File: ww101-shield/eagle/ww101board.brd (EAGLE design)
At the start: 53.3 x 60.6 mm, 6 parts, among them U1 LIGHTSENSORALS

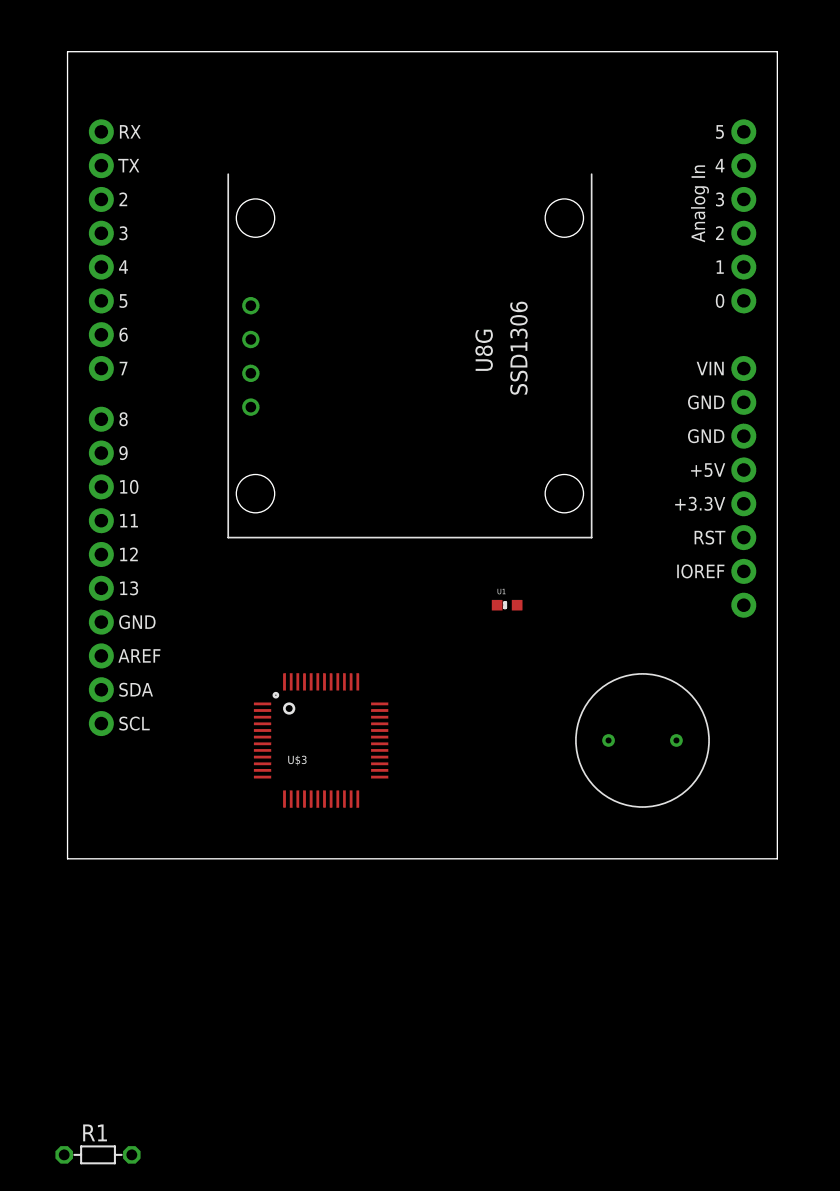
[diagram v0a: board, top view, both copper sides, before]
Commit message: Power routing done... now try signal routing
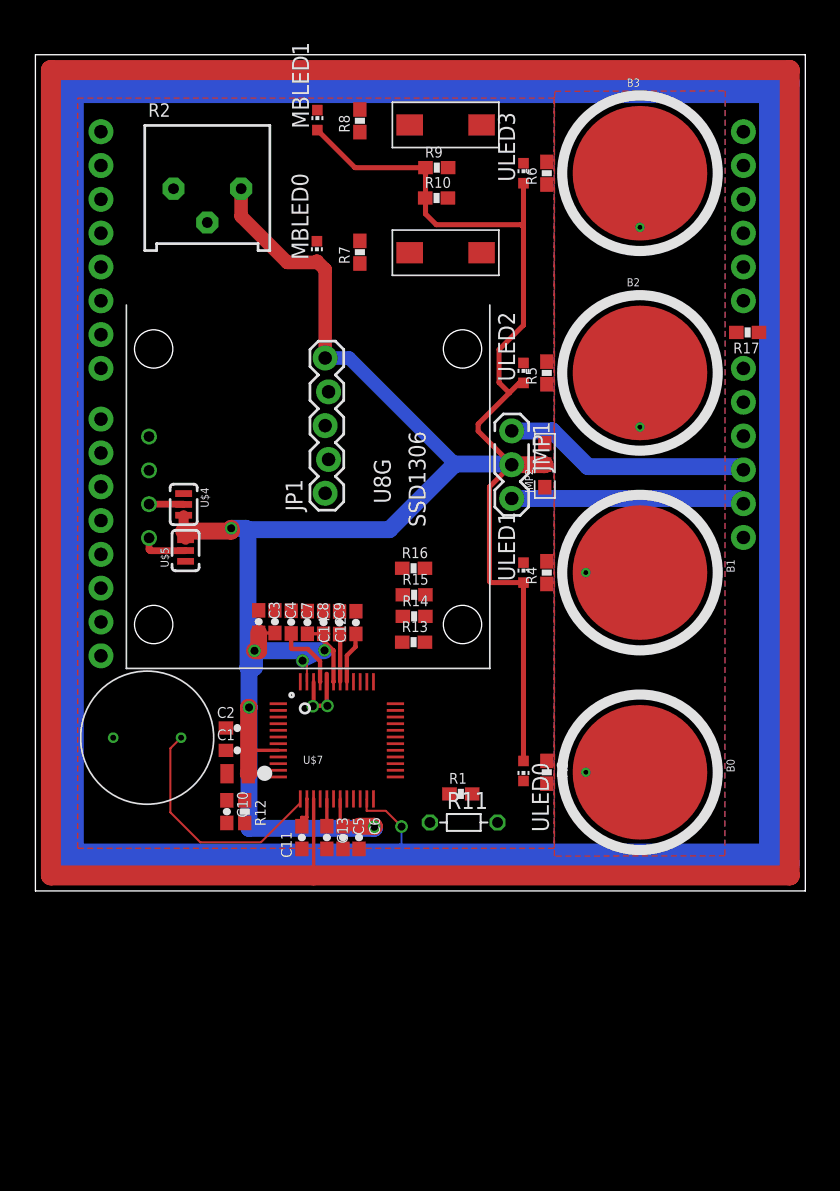
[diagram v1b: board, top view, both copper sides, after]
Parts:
- removed U$1: ARDUINO_R3_SHIELD, SparkFun-Boards:UNO_R3_SHIELD
- added ALS: ALS, IOTExpert:ALS
- added B0, B1, B2, B3: (no value), PatternAgents-TouchWidgets:BUTTON_PASSIVE_10MM
- added C1, C3, C5, C8: 1uF, PatternAgents-ProtoPads:0603-CAP
- added C10, C2, C4, C6, C7, C9: 0.1uF, PatternAgents-ProtoPads:0603-CAP
- added C11: 180pF, PatternAgents-ProtoPads:0603-CAP
- added C12, C13, C14: (no value), PatternAgents-ProtoPads:0603-CAP
- added JMP1: (no value), PatternAgents-ProtoPads:JMP-3-NO-PTH-2.54
- added JMP2: (no value), PatternAgents-ProtoPads:JMP-3-NO-0603
- added JP1: (no value), SparkFun-Connectors:1X05_LOCK
- added MB0, MB1: EVQPE1, IOTExpert:SWITCH
- added MBLED0, MBLED1, ULED0, ULED1, ULED2, ULED3: (no value), adafruit:CHIP-LED0603
- added R10, R9: 10K, PatternAgents-ProtoPads:0603-RES
- added R11: THERMISTOR-5, varistor:R-5
- added R12: 220K, PatternAgents-ProtoPads:0603-RES
- added R13, R14, R15, R16: 560, PatternAgents-ProtoPads:0603-RES
- added R17: 0, PatternAgents-ProtoPads:0603-RES
- added R2: (no value), pot:3386P
- added R3, R4, R5, R6, R7, R8: 330, PatternAgents-ProtoPads:0603-RES
- added U$5: JMP-3-2_3, PatternAgents-ProtoPads:JMP-3-2_3
- added U$7: CY8C4A45-48, PatternAgents-Cypress:TQFP-7X7-48
- R1: value THERMISTOR-5 -> (none); device varistor:R-5 -> PatternAgents-ProtoPads:0603-RES
- U$3: value CY8C4247AZI-L433 -> HPP801A031; device PatternAgents-Cypress:TQFP-7X7-48 -> IOTExpert:HUMIDITY
- U$4: value HPP801A031 -> JMP-3-1_2; device IOTExpert:HUMIDITY -> PatternAgents-ProtoPads:JMP-3-1_2
- U1: value LIGHTSENSORALS -> ARDUINO_SHIELDNOHOLESORLABELS; device SparkFun-Sensors:ALS-PT19 -> SparkFun-Boards:DUEMILANOVE_SHIELD_NOHOLES_NOLABELS
- moved R1 38.4 mm to (29.5, 4.88)
- moved U1 38.1 mm to (-0.03, 0.01)
- moved U$4 36.5 mm to (8.72, 26.6), turned to 270 degrees
- moved U$2 12.5 mm to (31.7, 14.3)
- moved U$3 10.5 mm to (8.53, 9.10), turned to 180 degrees
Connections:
- removed net P0_6: U$3.34
- removed net P1_2: U$3.44
- removed net P2_2: U$3.4
- removed net P2_6: U$3.8
- removed net P3_6: U$3.19
- removed net VDD: U$2.VDD
- new net A0: R17.1, U1.A0
- new net CAP-PROX: U$7.15
- new net CB0: R13.1, U$7.39
- new net CB1: R14.1, U$7.40
- new net CB2: R15.1, U$7.7
- new net CB3: R16.1, U$7.4
- new net CBLED0: R3.1, U$7.6
- new net CBLED1: R4.1, U$7.5
- new net CBLED2: R5.1, U$7.10
- new net CBLED3: R6.1, U$7.16
- new net CMOD: C12.1, U$7.41
- new net CSHIELD: U$7.23
- new net CTANK: C14.1, U$7.42
- new net D10: U$7.35, U1.D10
- new net D3: U$7.31, U1.D3
- new net D5: U$7.33, U1.D5
- new net D6: U1.D6
- new net D9: U$7.34, U1.D9
- new net H-REF-CAP: C11.2, U$7.14
- new net HUMIDITY: U$3.P$1, U$7.13
- new net MB0: MB0.P$2, R9.2, U$7.28
- new net MB1: MB1.P$2, R10.2, U$7.29
- new net MBLED0: R7.1, U$7.30
- new net MBLED1: R8.1, U$7.32
- new net N$10: R5.2, ULED2.C
- new net N$11: R6.2, ULED3.C
- new net N$12: MBLED0.C, R7.2
- new net N$13: MBLED1.C, R8.2
- new net N$14: U$2.VDD, U$4.2
- new net N$15: B3.BUTTON, R16.2
- new net N$17: U$2.GND, U$5.2
- new net N$2: B0.BUTTON, R13.2
- new net N$20: C7.2, U$7.45
- new net N$5: B1.BUTTON, R14.2
- new net N$7: B2.BUTTON, R15.2
- new net N$8: R3.2, ULED0.C
- new net N$9: R4.2, ULED1.C
- new net P30: U$7.20
- new net P31: U$7.21
- new net P32: U$7.22
- new net POT: R2.2, U$7.24, U1.A2
- new net SCL: U$2.SCL, U$7.37
- new net SCLK: JP1.2
- new net SDA: U$2.SDA, U$7.38
- new net SDAT: JP1.1
- new net THERM-LOW: R11.2, U$7.26
- new net THERM-MID: R1.1, R11.1, U$7.25
- new net THERM-REF-HIGH: R1.2, U$7.27, U$7.3
- new net TIA_IN: ALS.CATHODE, C10.1, R12.1, U$7.11
- new net TIA_OUT: C10.2, R12.2, R17.2, U$7.12
- new net UARTRX: U$7.1, U1.TX
- new net UARTTX: U$7.48, U1.RX
- new net V33: JMP1.3, JMP2.1, U1.3.3V
- new net V50: JMP1.1, JMP2.3, U1.5V
- new net VDAC: U$7.2, U1.A1
- new net VPWR: ALS.ANNODE, C1.2, C2.2, C3.2, C4.2, C5.1, C6.1, C8.2, C9.2, JMP1.2, JMP2.2, JP1.5, MBLED0.A, MBLED1.A, R10.1, R2.3, R9.1, U$4.3, U$5.3, U$7.19, U$7.43, U$7.47, U$7.8, ULED0.A, ULED1.A, ULED2.A, ULED3.A
- new net VREF: C13.1, U$7.17
- new net XRES: JP1.3, U$7.36, U1.RES
- net GND: now also C1.1, C11.1, C12.2, C13.2, C14.2, C2.1, C3.1, C4.1, C5.2, C6.2, C7.1, C8.1, C9.1, JP1.4, MB0.P$1, MB1.P$1, R2.1, U$3.P$2, U$4.1, U$5.1, U$7.18, U$7.44, U$7.46, U$7.9, U1.GND@0, U1.GND@1, U1.GND@2; no longer U$2.GND
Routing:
- net CAP-PROX: track 0.00 -> 237.8 mm
- net CSHIELD: track 0.00 -> 231.2 mm, vias 0 -> 1
- net VPWR: track 0.00 -> 196.9 mm, vias 0 -> 6
- net V50: track 0.00 -> 18.6 mm
- net HUMIDITY: track 0.00 -> 18.2 mm
- net V33: track 0.00 -> 17.6 mm
- net GND: track 0.00 -> 5.23 mm, vias 0 -> 2
- net N$20: track 0.00 -> 5.23 mm
- net CMOD: track 0.00 -> 3.88 mm
- net N$17: track 0.00 -> 3.65 mm
- net CTANK: track 0.00 -> 3.60 mm
- net N$14: track 0.00 -> 2.61 mm
- net H-REF-CAP: track 0.00 -> 2.43 mm
- net VREF: track 0.00 -> 2.05 mm
- added copper zone on layer 1, net GND
- added copper zone on layer 16, net GND
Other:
- board size 53.3 x 60.6 mm -> 57.8 x 62.8 mm

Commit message: first complete route of board
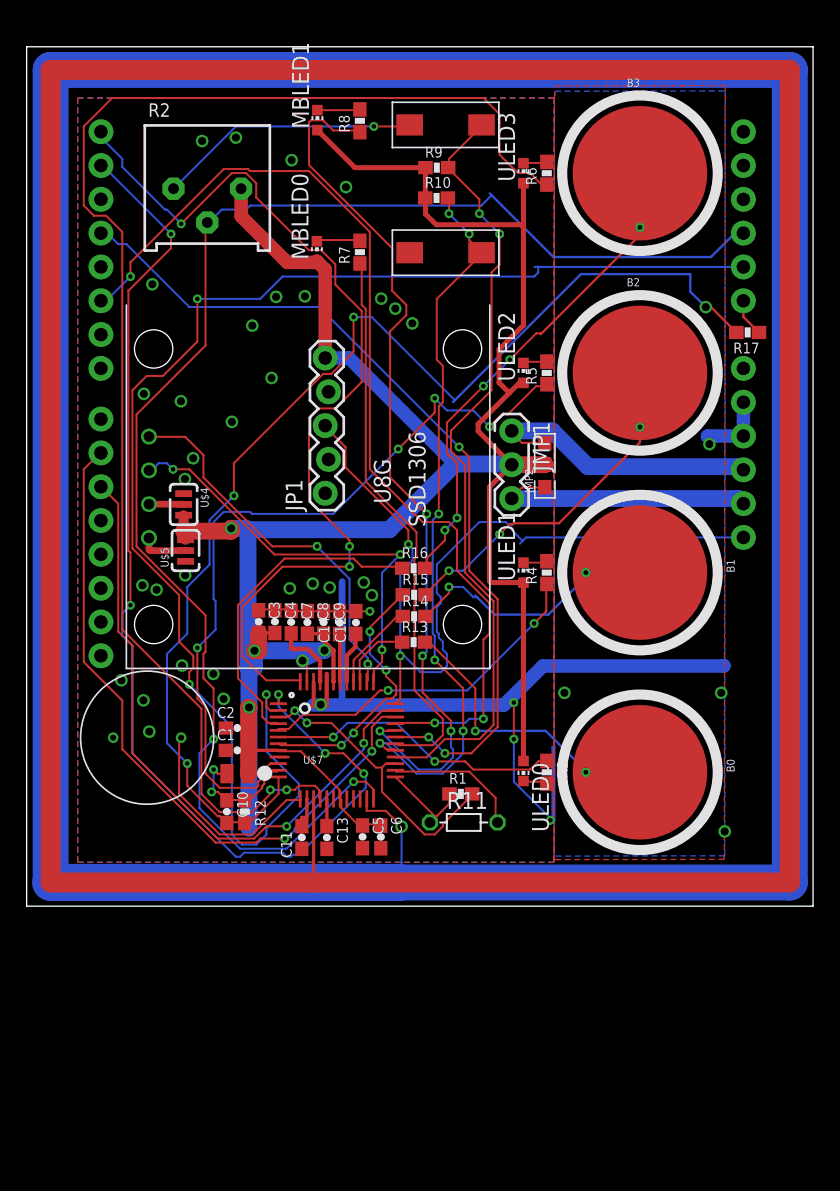
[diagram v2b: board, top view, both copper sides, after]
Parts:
- moved C6 1.64 mm to (23.5, 1.64)
- moved C5 1.47 mm to (22.2, 1.65)
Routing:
- net POT: track 0.00 -> 110.7 mm, vias 0 -> 2
- net VDAC: track 0.00 -> 106.6 mm, vias 0 -> 3
- net CBLED3: track 0.00 -> 105.8 mm, vias 0 -> 2
- net GND: track 5.23 -> 102.6 mm, vias 2 -> 41
- net TIA_OUT: track 0.00 -> 90.3 mm, vias 0 -> 4
- net UARTRX: track 0.00 -> 82.8 mm, vias 0 -> 5
- net D5: track 0.00 -> 75.3 mm, vias 0 -> 3
- net UARTTX: track 0.00 -> 71.6 mm, vias 0 -> 3
- net MBLED1: track 0.00 -> 66.0 mm, vias 0 -> 4
- net D3: track 0.00 -> 64.8 mm, vias 0 -> 3
- net XRES: track 0.00 -> 62.1 mm, vias 0 -> 2
- net MB0: track 0.00 -> 58.9 mm, vias 0 -> 2
- net CBLED2: track 0.00 -> 58.8 mm, vias 0 -> 4
- net MB1: track 0.00 -> 54.8 mm, vias 0 -> 6
- net D9: track 0.00 -> 52.5 mm, vias 0 -> 2
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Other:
- board size 57.8 x 62.8 mm -> 59.1 x 64.6 mm

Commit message: routing complete
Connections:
- removed net SCLK: JP1.2
- removed net SDAT: JP1.1
- net MB0: now also JP1.1
- net MB1: now also JP1.2
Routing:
- net MB1: track 54.8 -> 76.1 mm, vias 6 -> 7
- net MB0: track 58.9 -> 78.6 mm, vias 2 -> 5
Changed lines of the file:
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@@
 <layer number="17" name="Pads" color="2" fill="1" visible="yes" active="yes"/>
 <layer number="18" name="Vias" color="2" fill="1" visible="yes" active="yes"/>
-<layer number="19" name="Unrouted" color="6" fill="1" visible="no" active="yes"/>
+<layer number="19" name="Unrouted" color="6" fill="1" visible="yes" active="yes"/>
 <layer number="20" name="Dimension" color="15" fill="1" visible="yes" active="yes"/>
-<layer number="21" name="tPlace" color="7" fill="1" visible="no" active="yes"/>
+<layer number="21" name="tPlace" color="7" fill="1" visible="yes" active="yes"/>
 <layer number="22" name="bPlace" color="7" fill="1" visible="no" active="yes"/>
 <layer number="23" name="tOrigins" color="15" fill="1" visible="no" active="yes"/>
@@
 <wire x1="28.8036" y1="30.6324" x2="29.8704" y2="29.5656" width="0.1524" layer="1"/>
 <wire x1="28.8036" y1="32.1564" x2="28.8036" y2="30.6324" width="0.1524" layer="1"/>
-<wire x1="31.8516" y1="35.2044" x2="28.8036" y2="32.1564" width="0.1524" layer="1"/>
+<wire x1="31.8516" y1="35.2044" x2="29.1084" y2="32.4612" width="0.1524" layer="1"/>
+<wire x1="29.1084" y1="32.4612" x2="28.8036" y2="32.1564" width="0.1524" layer="1"/>
 <wire x1="31.8516" y1="44.0436" x2="31.8516" y2="35.2044" width="0.1524" layer="1"/>
 <wire x1="32.4612" y1="44.6532" x2="31.8516" y2="44.0436" width="0.1524" layer="1"/>
@@
 <via x="32.4612" y="46.9392" extent="1-16" drill="0.3302"/>
 <via x="30.9372" y="48.4632" extent="1-16" drill="0.3302"/>
+<contactref element="JP1" pad="1"/>
+<wire x1="19.812" y1="28.0416" x2="19.3548" y2="27.5844" width="0.1524" layer="16"/>
+<wire x1="19.812" y1="28.194" x2="19.812" y2="28.0416" width="0.1524" layer="16"/>
+<wire x1="20.2692" y1="28.6512" x2="19.812" y2="28.194" width="0.1524" layer="16"/>
+<wire x1="20.4216" y1="28.6512" x2="20.2692" y2="28.6512" width="0.1524" layer="16"/>
+<wire x1="23.3172" y1="31.5468" x2="20.4216" y2="28.6512" width="0.1524" layer="16"/>
+<wire x1="23.3172" y1="37.338" x2="23.3172" y2="31.5468" width="0.1524" layer="1"/>
+<wire x1="23.622" y1="37.6428" x2="23.3172" y2="37.338" width="0.1524" layer="1"/>
+<wire x1="28.8036" y1="32.4612" x2="23.622" y2="37.6428" width="0.1524" layer="16"/>
+<wire x1="29.1084" y1="32.4612" x2="28.8036" y2="32.4612" width="0.1524" layer="16"/>
+<wire x1="19.3548" y1="27.5844" x2="19.353" y2="27.46" width="0.1524" layer="16"/>
+<via x="23.3172" y="31.5468" extent="1-16" drill="0.3302"/>
+<via x="23.622" y="37.6428" extent="1-16" drill="0.3302"/>
+<via x="29.1084" y="32.4612" extent="1-16" drill="0.3302"/>
 </signal>
 <signal name="MB1">
@@
 <via x="27.5844" y="14.9352" extent="1-16" drill="0.3302"/>
 <via x="27.8892" y="25.908" extent="1-16" drill="0.3302"/>
+<contactref element="JP1" pad="2"/>
+<wire x1="19.6596" y1="28.956" x2="19.6596" y2="29.8704" width="0.1524" layer="1"/>
+<wire x1="24.5364" y1="24.0792" x2="19.6596" y2="28.956" width="0.1524" layer="1"/>
+<wire x1="24.5364" y1="23.622" x2="24.5364" y2="24.0792" width="0.1524" layer="1"/>
+<wire x1="25.146" y1="24.2316" x2="24.5364" y2="23.622" width="0.1524" layer="16"/>
+<wire x1="25.908" y1="24.2316" x2="25.146" y2="24.2316" width="0.1524" layer="16"/>
+<wire x1="26.2128" y1="23.9268" x2="25.908" y2="24.2316" width="0.1524" layer="16"/>
+<wire x1="26.2128" y1="15.6972" x2="26.2128" y2="23.9268" width="0.1524" layer="16"/>
+<wire x1="26.0604" y1="15.5448" x2="26.2128" y2="15.6972" width="0.1524" layer="16"/>
+<wire x1="26.0604" y1="14.9352" x2="26.0604" y2="15.5448" width="0.1524" layer="16"/>
+<wire x1="26.3652" y1="14.6304" x2="26.0604" y2="14.9352" width="0.1524" layer="16"/>
+<wire x1="27.2796" y1="14.6304" x2="26.3652" y2="14.6304" width="0.1524" layer="16"/>
+<wire x1="27.5844" y1="14.9352" x2="27.2796" y2="14.6304" width="0.1524" layer="16"/>
+<wire x1="19.6596" y1="29.8704" x2="19.607" y2="30" width="0.1524" layer="1"/>
+<via x="24.5364" y="23.622" extent="1-16" drill="0.3302"/>
 </signal>
 <signal name="N$12">
@@
 <via x="7.7724" y="46.9392" extent="1-16" drill="0.3302"/>
 </signal>
-<signal name="SDAT">
-<contactref element="JP1" pad="1"/>
-</signal>
-<signal name="SCLK">
-<contactref element="JP1" pad="2"/>
-</signal>
 <signal name="CB3">

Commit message: First complete board
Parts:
- removed JMP2: (no value), PatternAgents-ProtoPads:JMP-3-NO-0603
- removed U$4: JMP-3-1_2, PatternAgents-ProtoPads:JMP-3-1_2
- added JPWR: 0, PatternAgents-ProtoPads:JMP-3-NO-0603
- added R18, R19, R20, R21: 10K, PatternAgents-ProtoPads:0603-RES
- added R30: JMP-3-1_2, PatternAgents-ProtoPads:JMP-3-1_2
- B0, B1, B2, B3: value (none) -> B
- C12: value (none) -> 2.2nF
- C13: value (none) -> 1uF
- C14: value (none) -> 10nF
- JMP1, JP1: value (none) -> 0
- MBLED0, MBLED1, ULED0, ULED1, ULED2, ULED3: value (none) -> red
- R1, R2: value (none) -> 10K
- renumbered ALS to D1, U$3 to HUMIDITY, U$5 to R31
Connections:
- removed net D6: U1.D6
- removed net P30: U$7.20
- removed net P31: U$7.21
- removed net P32: U$7.22
- net GND: now also R30.3; no longer U$4.1
- net N$14: now also R30.2; no longer U$4.2
- net SCL: now also R18.1, R19.1
- net SDA: now also R20.1, R21.1
- net V33: now also JPWR.3; no longer JMP2.1
- net V50: now also JPWR.1; no longer JMP2.3
- net VPWR: now also JPWR.2, R18.2, R19.2, R20.2, R21.2, R30.1; no longer JMP2.2, U$4.3
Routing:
- net GND: track 102.6 -> 130.6 mm, vias 41 -> 106
- net SCL: track 32.4 -> 46.6 mm, vias 3 -> 4
- net VPWR: track 193.7 -> 204.5 mm
- net SDA: track 28.8 -> 39.1 mm, vias 2 -> 3
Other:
- board text added: "A0 TIA"
- board text added: "A1 DAC"
- board text added: "A2 POT"
- board text added: "D1"
- board text added: "D10 P07"
- board text added: "D3 P03"
- board text added: "D5 P05"
- board text added: "D9 P06"
- board text added: "GND"
- board text added: "H1"
- board text added: "MB0"
- board text added: "MB1"
- board text added: "RX P10"
- board text added: "SCLK"
- board text added: "SDAT"
- board text added: "TX P11"
- board text added: "V33"
- board text added: "V50"
- board text added: "VPWR"
- board text added: "XRES"

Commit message: Fixed resistors
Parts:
- R3, R4, R5, R6, R7, R8: value 330 -> 560
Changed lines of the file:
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@@
 <layer number="19" name="Unrouted" color="6" fill="1" visible="no" active="yes"/>
 <layer number="20" name="Dimension" color="15" fill="1" visible="no" active="yes"/>
-<layer number="21" name="tPlace" color="7" fill="1" visible="no" active="yes"/>
+<layer number="21" name="tPlace" color="7" fill="1" visible="yes" active="yes"/>
 <layer number="22" name="bPlace" color="7" fill="1" visible="no" active="yes"/>
 <layer number="23" name="tOrigins" color="15" fill="1" visible="no" active="yes"/>
@@
 <attribute name="VALUE" x="36.155" y="50.865" size="1.27" layer="27" rot="R90"/>
 </element>
-<element name="R3" library="PatternAgents-ProtoPads" package="0603-RES" value="330" x="36" y="6.5" locked="yes" smashed="yes" rot="R270">
+<element name="R3" library="PatternAgents-ProtoPads" package="0603-RES" value="560" x="36" y="6.5" locked="yes" smashed="yes" rot="R270">
 <attribute name="NAME" x="35.746" y="5.0268" size="0.8128" layer="25" font="vector" ratio="15" rot="R270"/>
 <attribute name="VALUE" x="34.349" y="8.024" size="0.6096" layer="27" font="vector" ratio="15" rot="R270"/>
 </element>
-<element name="R4" library="PatternAgents-ProtoPads" package="0603-RES" value="330" x="36" y="21.5" locked="yes" smashed="yes" rot="R90">
+<element name="R4" library="PatternAgents-ProtoPads" package="0603-RES" value="560" x="36" y="21.5" locked="yes" smashed="yes" rot="R90">
 <attribute name="NAME" x="36.3556" y="18.579" size="0.8128" layer="25" font="vector" ratio="15" rot="R90"/>
 <attribute name="VALUE" x="37.651" y="19.976" size="0.6096" layer="27" font="vector" ratio="15" rot="R90"/>
 </element>
-<element name="R5" library="PatternAgents-ProtoPads" package="0603-RES" value="330" x="36" y="36.5" locked="yes" smashed="yes" rot="R90">
+<element name="R5" library="PatternAgents-ProtoPads" package="0603-RES" value="560" x="36" y="36.5" locked="yes" smashed="yes" rot="R90">
 <attribute name="NAME" x="36.7536" y="34.8062" size="0.8128" layer="25" font="vector" ratio="15" rot="R180"/>
 <attribute name="VALUE" x="37.651" y="34.976" size="0.6096" layer="27" font="vector" ratio="15" rot="R90"/>
 </element>
-<element name="R6" library="PatternAgents-ProtoPads" package="0603-RES" value="330" x="36" y="51.5" locked="yes" smashed="yes" rot="R90">
+<element name="R6" library="PatternAgents-ProtoPads" package="0603-RES" value="560" x="36" y="51.5" locked="yes" smashed="yes" rot="R90">
 <attribute name="NAME" x="36.7904" y="49.7922" size="0.8128" layer="25" font="vector" ratio="15" rot="R180"/>
 <attribute name="VALUE" x="37.651" y="49.976" size="0.6096" layer="27" font="vector" ratio="15" rot="R90"/>
 </element>
-<element name="R7" library="PatternAgents-ProtoPads" package="0603-RES" value="330" x="21.96" y="45.57" locked="yes" rot="R90"/>
-<element name="R8" library="PatternAgents-ProtoPads" package="0603-RES" value="330" x="21.96" y="55.44" locked="yes" rot="R90"/>
+<element name="R7" library="PatternAgents-ProtoPads" package="0603-RES" value="560" x="21.96" y="45.57" locked="yes" rot="R90"/>
+<element name="R8" library="PatternAgents-ProtoPads" package="0603-RES" value="560" x="21.96" y="55.44" locked="yes" rot="R90"/>
 <element name="JMP1" library="PatternAgents-ProtoPads" package="JMP-3-NO-PTH-2.54" value="0" x="33.3669" y="32.145678125" locked="yes" smashed="yes" rot="R270">
 <attribute name="NAME" x="30.1919" y="31.612278125" size="1.27" layer="25" font="vector" ratio="15" rot="R270"/>
